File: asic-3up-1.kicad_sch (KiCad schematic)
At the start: 64 parts, among them J5 Conn_01x01, J7 Conn_01x01, U48 MCP1824T-1202E/OT, U49 MCP1824T-1202E/OT, U50 MCP1824T-1202E/OT, U51 MCP1824T-0802E, U52 MCP1824T-0802E, U53 MCP1824T-0802E, U54 BM1362AC_MODE1, U55 BM1362AC_MODE0, U56 BM1362AC_MODE1

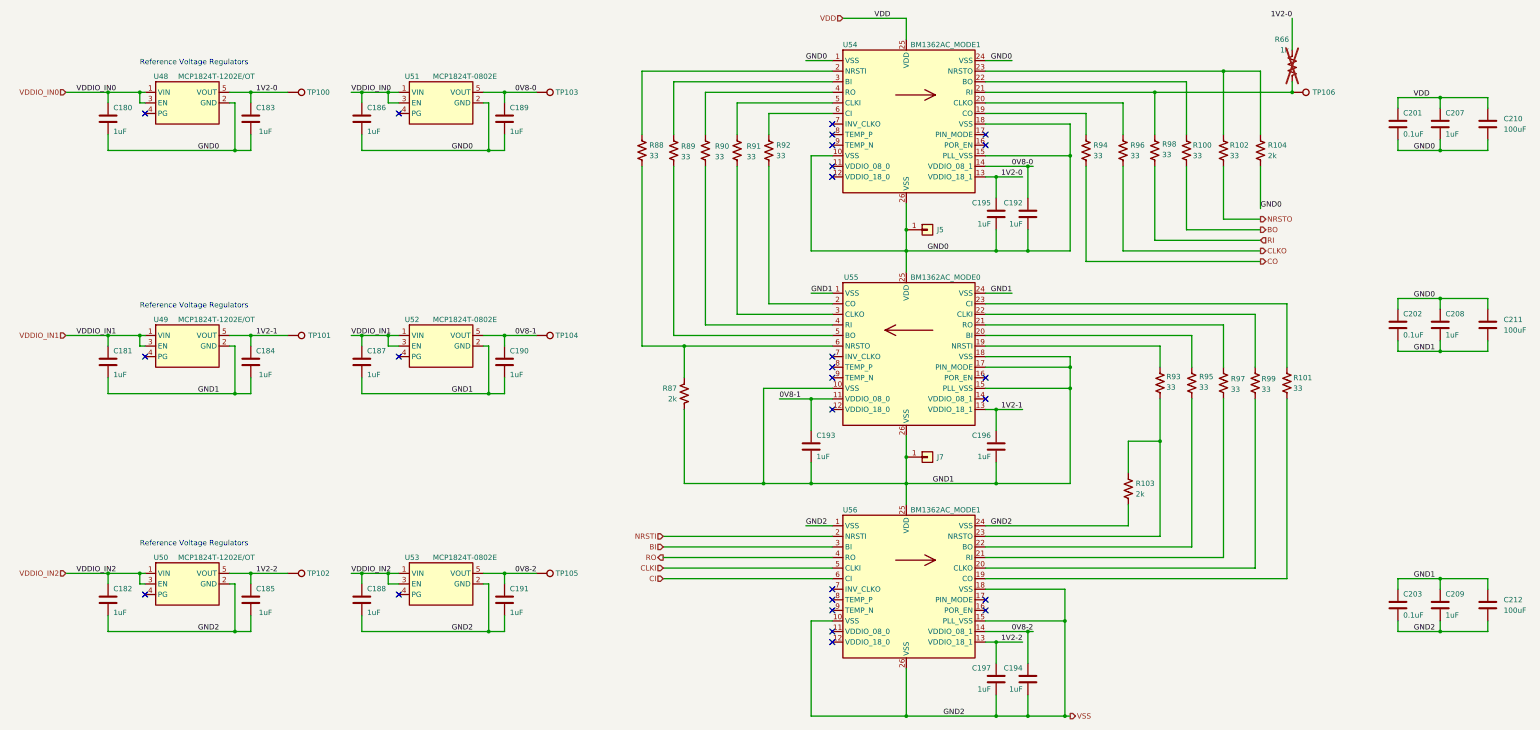
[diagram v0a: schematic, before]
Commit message: added topside data test pads. cleaned up power pads some more.
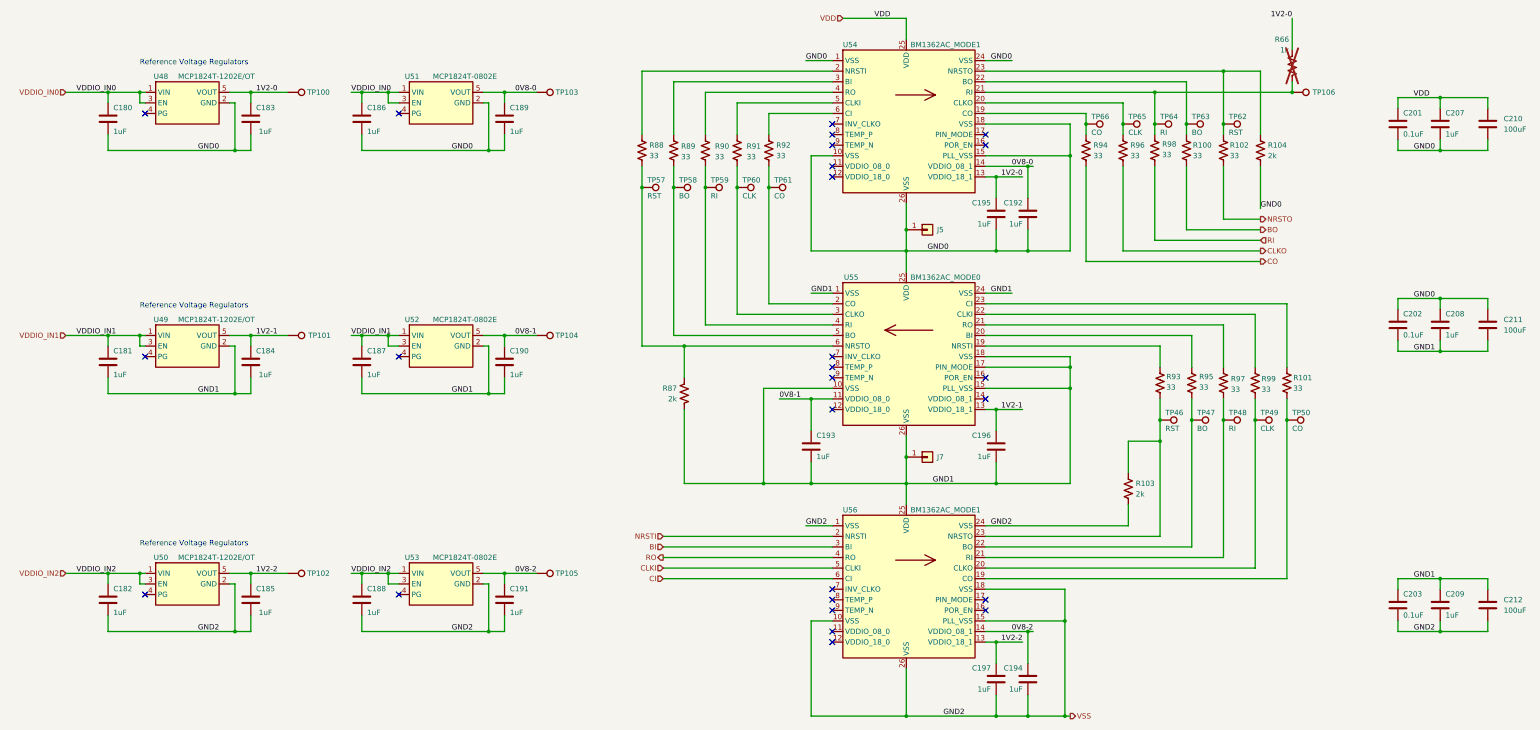
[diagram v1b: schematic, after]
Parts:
- added TP46, TP57, TP62: RST, emberone:TestPoint_Pad_1.0x0.4mm, symbol Connector:TestPoint
- added TP47, TP58, TP63: BO, emberone:TestPoint_Pad_1.0x0.4mm, symbol Connector:TestPoint
- added TP48, TP59, TP64: RI, emberone:TestPoint_Pad_1.0x0.4mm, symbol Connector:TestPoint
- added TP49, TP60, TP65: CLK, emberone:TestPoint_Pad_1.0x0.4mm, symbol Connector:TestPoint
- added TP50, TP61, TP66: CO, emberone:TestPoint_Pad_1.0x0.4mm, symbol Connector:TestPoint
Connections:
- net at R95.2, U56.22 (BO): now also TP47.1
- net at R101.2, U56.19 (CO): now also TP50.1
- net at R92.2, U55.2 (CO): now also TP61.1
- net at R96.1, U54.20 (CLKO): now also TP65.1
- net at R94.1, U54.19 (CO): now also TP66.1
- net at R66.2, R98.1, TP106.1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: now also TP64.1
- net at R100.1, U54.22 (BO): now also TP63.1
- net at R102.1, R104.1, U54.23 (NRSTO): now also TP62.1
- net at R103.1, R93.2, U56.23 (NRSTO): now also TP46.1
- net at R91.2, U55.3 (CLKO): now also TP60.1
- net at R90.2, U55.4 (RI): now also TP59.1
- net at R89.2, U55.5 (BO): now also TP58.1
- net at R87.1, R88.2, U55.6 (NRSTO): now also TP57.1
- net at R99.2, U56.20 (CLKO): now also TP49.1
- net at R97.2, U56.21 (RI): now also TP48.1

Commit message: add BOM, iBOM and position files
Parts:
- J5, J7: now left out of the parts list
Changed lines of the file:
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@@
 		(unit 1)
 		(exclude_from_sim no)
-		(in_bom yes)
+		(in_bom no)
 		(on_board yes)
 		(dnp no)
@@
 		(unit 1)
 		(exclude_from_sim no)
-		(in_bom yes)
-		(on_board yes)
-		(dnp no)
+		(in_bom no)
+		(on_board yes)
+		(dnp no)

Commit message: corrected the voltage regulator input and output capacitors. Updated BOM, iBOM, cpos, gerbers and render.
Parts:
- U54, U55, U56: PARTNO (none) -> BM1362AC
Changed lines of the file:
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@@
+			)
+		)
+		(property "PARTNO" "BM1362AC"
+			(at 248.92 72.39 0)
+			(effects
+				(font
+					(size 1.27 1.27)
+				)
+				(hide yes)
 			)
 		)
@@
 			)
 		)
+		(property "PARTNO" "BM1362AC"
+			(at 248.92 128.27 0)
+			(effects
+				(font
+					(size 1.27 1.27)
+				)
+				(hide yes)
+			)
+		)
 		(pin "10"
 		)
@@
 			(at 248.92 184.15 0)
 			(effects
+				(font
+					(size 1.27 1.27)
+				)
+				(hide yes)
+			)
+		)
+		(property "PARTNO" "BM1362AC"
+			(at 248.92 184.15 0)
+			(effects

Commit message: bump version to v6
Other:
- company: (none) -> 256Foundation
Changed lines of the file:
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@@
 	(title_block
 		(title "emberOne/00")
-		(date "2025-09-17")
-		(rev "5")
+		(date "2026-02-17")
+		(rev "v6")
+		(company "256Foundation")
+		(comment 1 "OHL-S-2.0")
 	)
 	(text "Reference Voltage Regulators"
